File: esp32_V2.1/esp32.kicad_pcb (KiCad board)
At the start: 2 copper layers, 80 x 66 mm, 75 parts, among them IC1 KF33BD-TR, J1 USB_C, Q2 8205A, Q3 BC817, Q4 BC817, SW1 Reset, SW2 Boot, U1 CH340G, U2 TC4056, U3 DW01A, U4 LM358, U5 TLC272, U6 LM358, X1 12 MHz

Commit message: Finished routing
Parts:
- removed the R5 at (117.0, 106.7)
- moved J4 72.7 mm to (153.4, 93.7)
- moved C11 69.0 mm to (161.3, 108.6)
- moved C12 69.0 mm to (161.3, 105.1)
- moved J5 69.0 mm to (132.1, 93.7)
- moved R19 65.8 mm to (142.0, 109.7)
- moved R20 65.8 mm to (130.8, 99.6)
- moved R21 65.8 mm to (130.8, 109.7)
- moved R22 65.8 mm to (136.4, 99.6)
- moved R23 65.8 mm to (136.4, 109.7)
- moved R26 65.8 mm to (142.0, 99.6)
- moved U4 65.8 mm to (142.0, 104.6)
- moved U6 65.8 mm to (130.8, 104.6)
- moved R24 65.8 mm to (147.6, 99.6)
- moved R25 65.8 mm to (153.2, 109.7)
- moved R5 65.8 mm to (147.6, 109.7)
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- renumbered pH to J4, ORP to J5, NTC to TH2
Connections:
- ESP32 pad 39: (no net) -> GND
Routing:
- net GND: track 176.5 -> 319.0 mm
- net Bat: track 0.00 -> 74.2 mm, vias 0 -> 2
- net EN: track 4.14 -> 75.8 mm, vias 0 -> 3
- net +3V3: track 13.3 -> 78.6 mm
- net Net-(R7-Pad2): track 58.9 -> 22.4 mm, vias 1 -> 0
- net Vcc: track 22.3 -> 48.0 mm
- net Net-(R4-Pad2): track 2.61 -> 26.4 mm, vias 1 -> 2
- net VBUS: track 38.9 -> 62.3 mm, vias 2 -> 3
- net Batt-: track 45.6 -> 23.2 mm
- net ORP-: track 17.5 -> 35.8 mm
- net Temp: track 5.89 -> 24.0 mm, vias 0 -> 2
- net Cl: track 1.27 -> 17.1 mm
- net Net-(Q3-Pad1): track 13.1 -> 25.7 mm
- net Net-(R20-Pad2): track 23.9 -> 11.7 mm
- net Net-(C9-Pad1): track 12.2 -> 24.0 mm
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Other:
- net class Default: clearance 0.25 -> 0.2
- rule trace_clearance: 0.25 -> 0.2

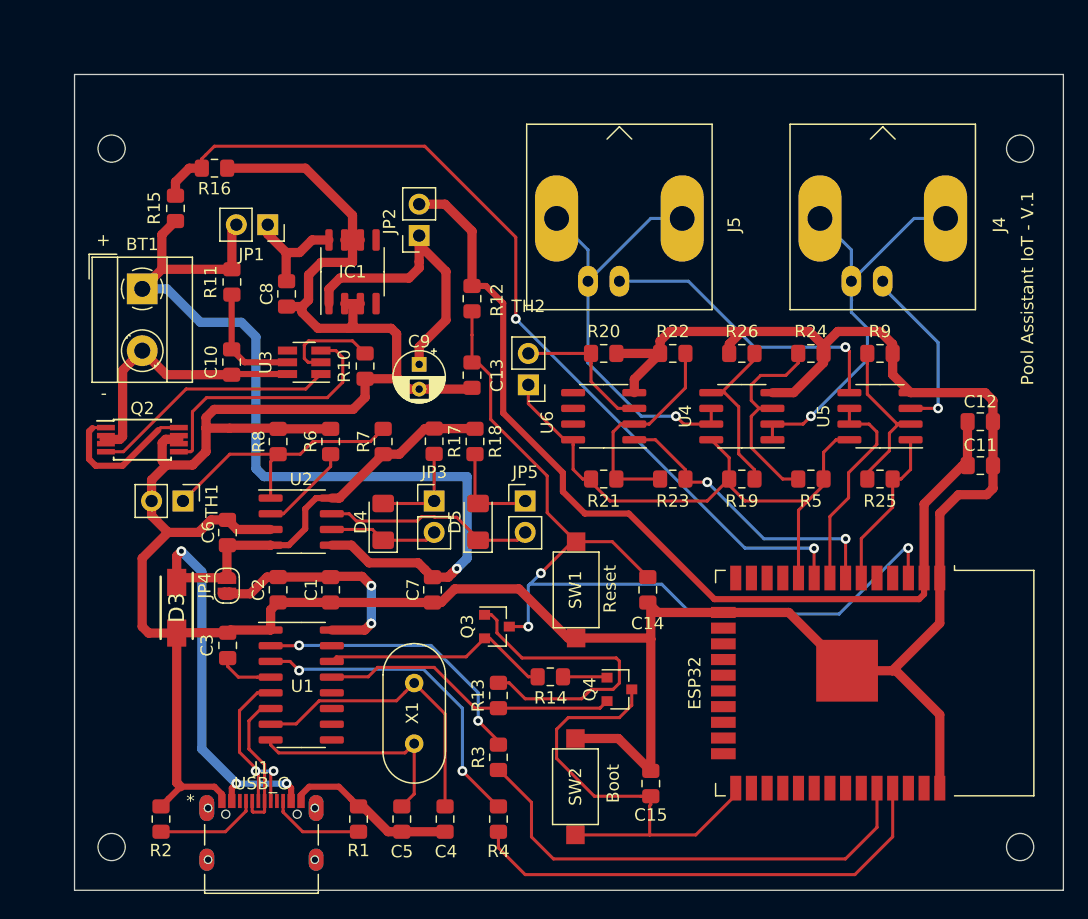
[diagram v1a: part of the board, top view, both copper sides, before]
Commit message: Made final changes. Added jumpers for Vcc, bat and buttons
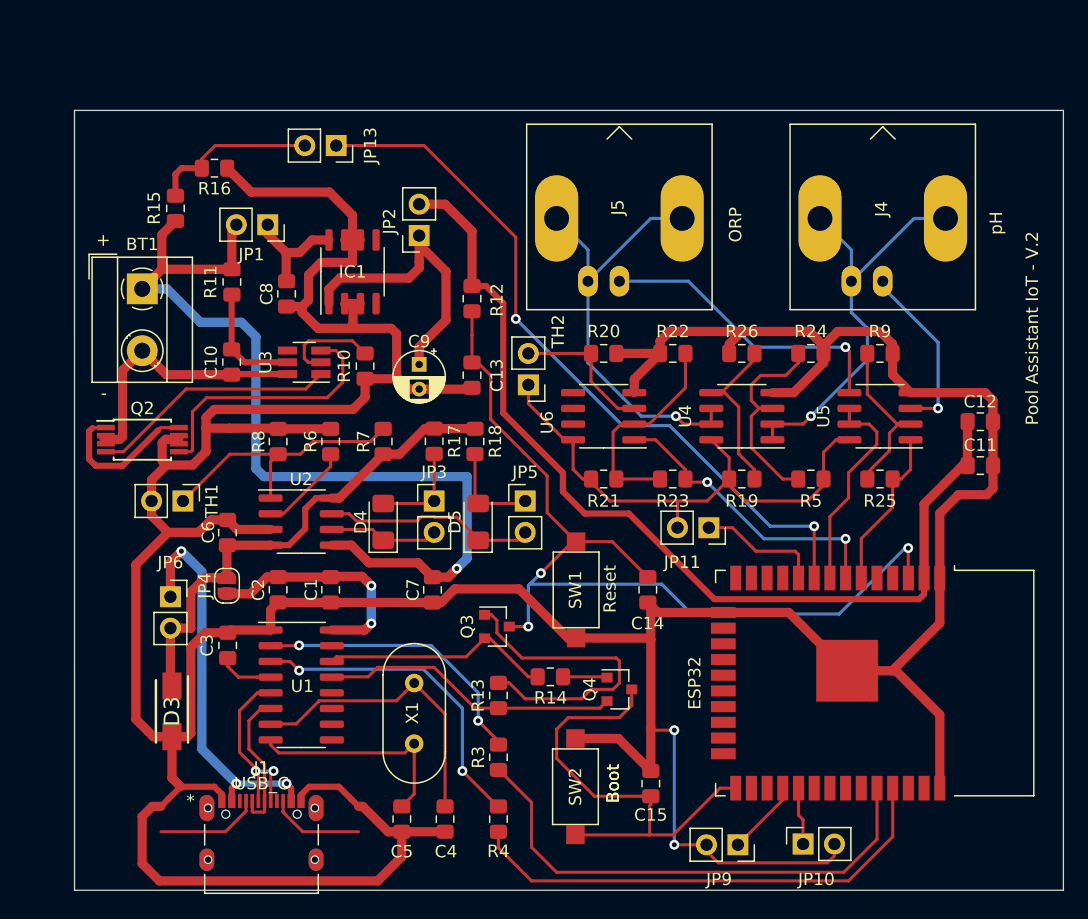
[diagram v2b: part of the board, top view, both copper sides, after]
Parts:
- removed G***: LOGO, FIUBA:FIUBA
- removed Hole1, Hole2, Hole3, Hole4: MountingHole_2.2mm_M2_ISO7380, MountingHole:MountingHole_2.2mm_M2_ISO7380
- removed R1, R2: 5.1k, Resistor_SMD:R_0805_2012Metric_Pad1.15x1.40mm_HandSolder
- added JP10: Jumper_NO, Connector_PinSocket_2.54mm:PinSocket_1x02_P2.54mm_Vertical, F.Cu at (146.9, 139.3)
- added JP11: Jumper_NO, Connector_PinSocket_2.54mm:PinSocket_1x02_P2.54mm_Vertical, F.Cu at (139.3, 113.7)
- added JP13: Jumper_NO, Connector_PinSocket_2.54mm:PinSocket_1x02_P2.54mm_Vertical, F.Cu at (109.2, 82.8)
- added JP6: Jumper_NO, Connector_PinSocket_2.54mm:PinSocket_1x02_P2.54mm_Vertical, F.Cu at (95.8, 119.3)
- added JP9: Jumper_NO, Connector_PinSocket_2.54mm:PinSocket_1x02_P2.54mm_Vertical, F.Cu at (141.7, 139.3)
- moved D3 8.39 mm to (95.9, 128.5)
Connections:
- ESP32 pad 10: Vcc -> Net-(ESP32-Pad10)
- J1 pad A4-B9: VBUS -> Net-(J1-PadA4-B9)
- J1 pad B4-A9: VBUS -> Net-(J1-PadA4-B9)
- R15 pad 2: Bat -> Net-(JP13-Pad2)
- R16 pad 1: Bat -> Net-(JP13-Pad2)
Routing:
- net GND: track 319.0 -> 383.2 mm, vias 0 -> 2
- net Net-(J1-PadA4-B9): track 0.00 -> 31.9 mm, vias 0 -> 3
- net VBUS: track 62.3 -> 40.2 mm, vias 3 -> 0
- net Bat: track 74.2 -> 59.5 mm
- net Net-(JP13-Pad2): track 0.00 -> 13.6 mm
- net Net-(ESP32-Pad10): track 0.00 -> 10.1 mm
- net 28: track 0.00 -> 6.09 mm
- net 29: track 0.00 -> 4.67 mm
- net Vcc: track 48.0 -> 43.6 mm
- net Rx: track 39.5 -> 41.4 mm
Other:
- board size 80 x 66 mm -> 80 x 63.1 mm
- board text added: "ORP"
- board text added: "Pool Assistant IoT - V.2"
- board text added: "pH"
- board text removed: "Pool Assistant IoT - V.1"

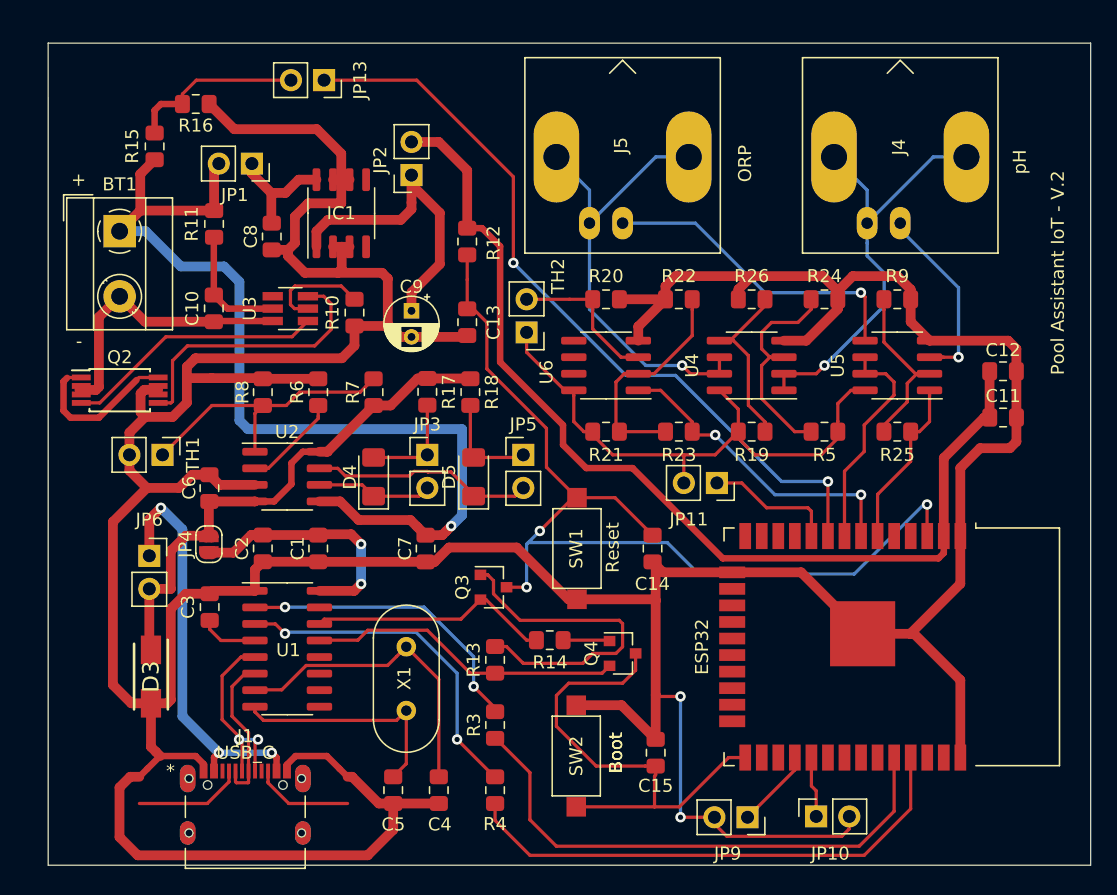
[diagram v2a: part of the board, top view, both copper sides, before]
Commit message: Add Holes, R1 and R2 to V2.1
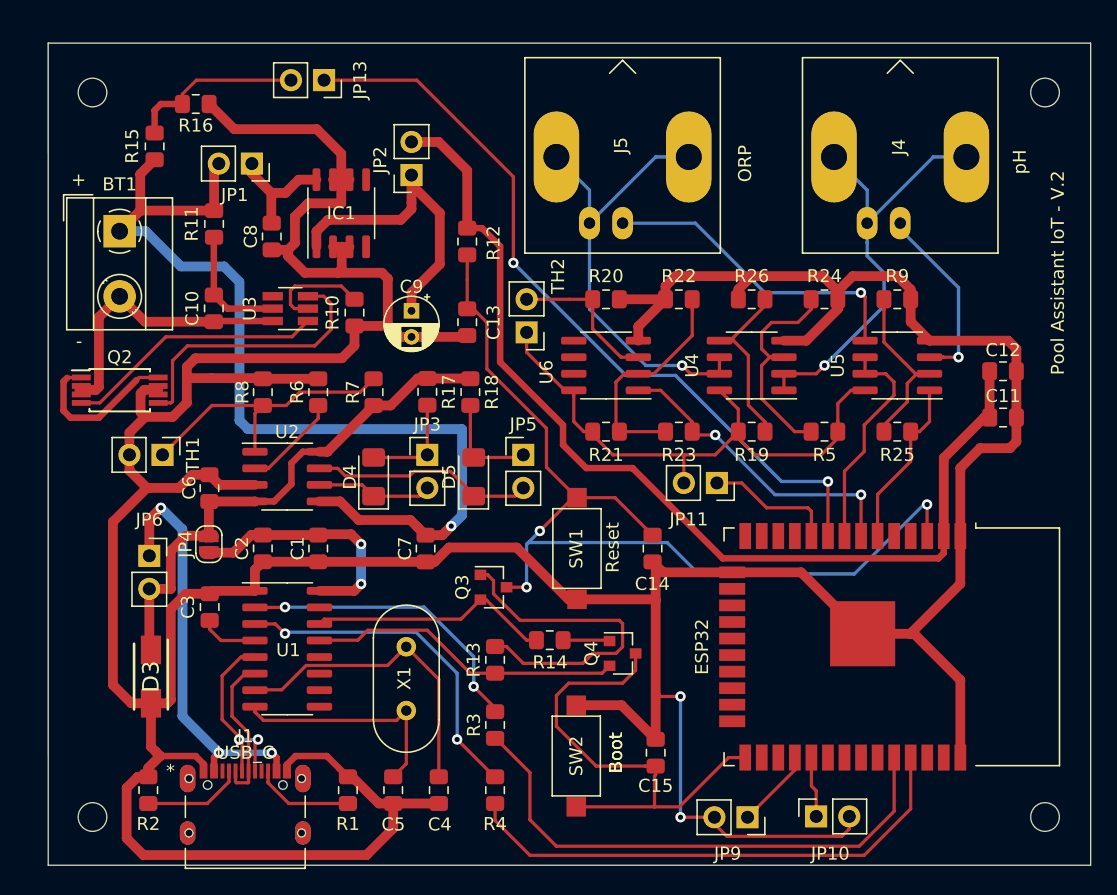
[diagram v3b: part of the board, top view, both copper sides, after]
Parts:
- added G***: LOGO, FIUBA:FIUBA, B.Cu at (151.9, 123.0)
- added Hole2: MountingHole_2.2mm_M2_ISO7380, MountingHole:MountingHole_2.2mm_M2_ISO7380, F.Cu at (164.5, 83.7)
- added Hole2: MountingHole_2.2mm_M2_ISO7380, MountingHole:MountingHole_2.2mm_M2_ISO7380, F.Cu at (164.5, 139.3)
- added Hole2: MountingHole_2.2mm_M2_ISO7380, MountingHole:MountingHole_2.2mm_M2_ISO7380, F.Cu at (91.4, 139.3)
- added Hole2: MountingHole_2.2mm_M2_ISO7380, MountingHole:MountingHole_2.2mm_M2_ISO7380, F.Cu at (91.4, 83.7)
- added R1: 5.1k, Resistor_SMD:R_0805_2012Metric_Pad1.15x1.40mm_HandSolder, F.Cu at (111.0, 137.2)
- added R2: 5.1k, Resistor_SMD:R_0805_2012Metric_Pad1.15x1.40mm_HandSolder, F.Cu at (95.7, 137.2)
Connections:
- ESP32 pad 39: GND -> (no net)
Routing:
- net GND: track 383.2 -> 382.5 mm
- net Net-(J1-PadA5): track 8.39 -> 7.71 mm

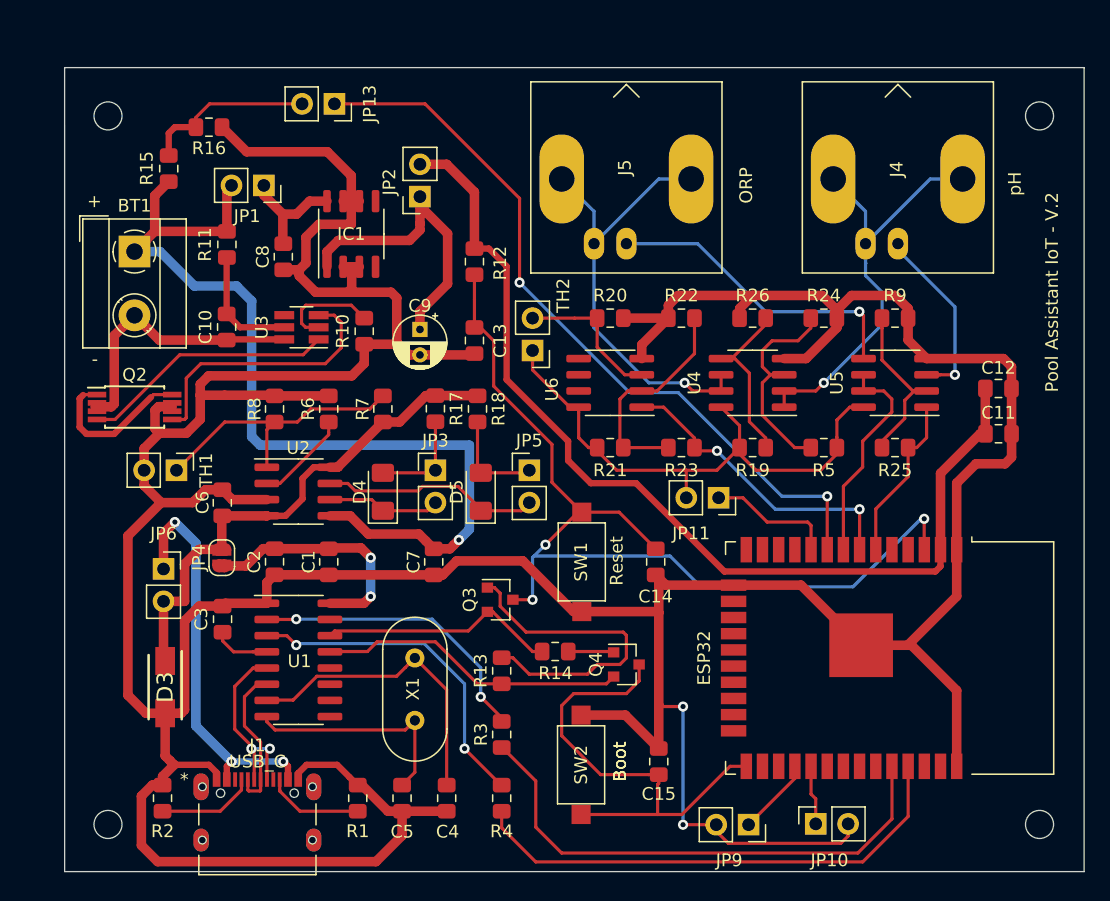
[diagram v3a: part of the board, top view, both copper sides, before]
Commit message: Refactor some tracks
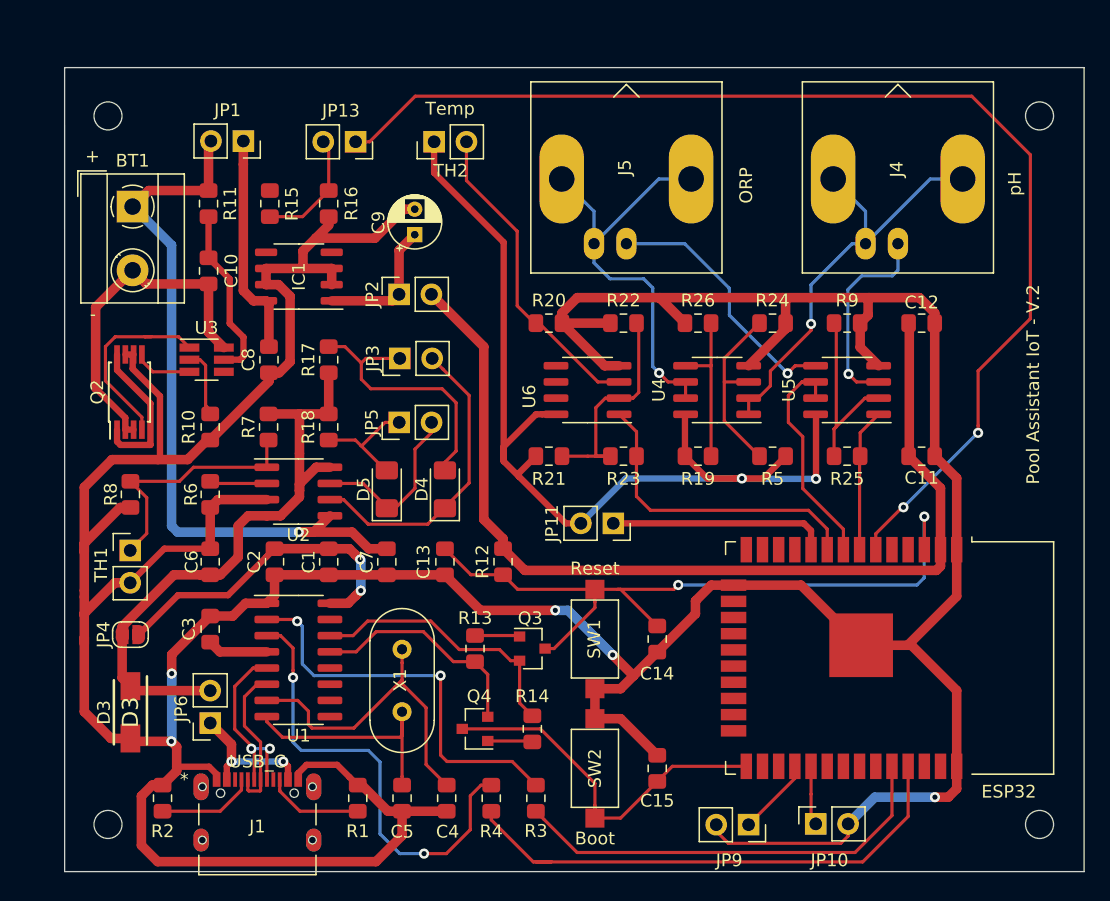
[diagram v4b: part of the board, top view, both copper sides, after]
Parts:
- moved R12 23.7 mm to (122.4, 118.7)
- moved TH2 18.1 mm to (117.0, 85.7), turned to 90 degrees
- moved C13 17.5 mm to (117.8, 118.7)
- moved R10 14.2 mm to (99.4, 108.1)
- moved R8 13.1 mm to (93.2, 113.4), turned to 270 degrees
- moved Q4 12.9 mm to (120.2, 131.8), turned to 180 degrees
- moved JP6 12.6 mm to (99.4, 131.3), turned to 180 degrees
- moved R18 11.8 mm to (108.7, 108.1)
- moved R6 11.5 mm to (99.4, 113.4), turned to 270 degrees
- moved R16 11.1 mm to (108.7, 90.6), turned to 270 degrees
- moved JP5 10.9 mm to (114.2, 107.8), turned to 90 degrees
- moved JP4 9.37 mm to (93.2, 124.4), turned to 180 degrees
- moved R17 9.21 mm to (108.7, 102.8), turned to 90 degrees
- moved JP3 9.21 mm to (114.3, 102.7), turned to 90 degrees
- moved R7 9.08 mm to (104.0, 108.1), turned to 270 degrees
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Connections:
- ESP32 pad 6: pH -> Bat
- ESP32 pad 7: Temp -> pH
- ESP32 pad 9: Bat -> Temp
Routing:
- net Vcc: track 43.6 -> 81.5 mm, vias 0 -> 2
- net Bat: track 59.5 -> 92.4 mm
- net Net-(Q3-Pad1): track 25.7 -> 3.53 mm
- net Net-(J1-PadA4-B9): track 31.9 -> 10.9 mm, vias 3 -> 2
- net EN: track 75.8 -> 57.7 mm, vias 3 -> 2
- net Net-(Q2-Pad5): track 21.4 -> 4.59 mm
- net Batt+: track 74.1 -> 57.6 mm
- net Net-(D4-Pad1): track 8.90 -> 24.0 mm
- net Net-(D4-Pad2): track 8.02 -> 21.5 mm
- net Net-(C9-Pad1): track 24.0 -> 10.7 mm
- net Net-(R20-Pad2): track 11.7 -> 25.0 mm
- net GND: track 382.5 -> 370.6 mm, vias 2 -> 5
- net Net-(R4-Pad2): track 26.4 -> 36.1 mm
- net Boot: track 37.1 -> 28.5 mm
- net Net-(R3-Pad2): track 23.3 -> 31.9 mm
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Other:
- net class Default: clearance 0.2 -> 0.25
- rule trace_clearance: 0.2 -> 0.25
- board text added: "D3"
- board text added: "Temp"
